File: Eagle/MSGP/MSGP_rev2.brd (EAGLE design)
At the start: 71.8 x 43.9 mm, 42 parts, among them IC1 74ALS04D, IC2 NE5532D, IC3 74ALS04D, IC4 74ALS04D, U1 LTC6905CS5TRMPBF

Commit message: Updates to Layout/Schem
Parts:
- added JP11, JP14, JP15: (no value), jumper:JP1
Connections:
- new net N$15: IC4.14, JP11.1
- new net N$22: IC1.14, JP14.1
- new net N$28: IC3.14, JP15.1
- net VCC: now also JP11.2, JP14.2, JP15.2; no longer IC1.14, IC3.14, IC4.14
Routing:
- net VCC: track 174.4 -> 165.8 mm
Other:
- board size 71.8 x 43.9 mm -> 81 x 57 mm
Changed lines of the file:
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@@
 <board>
 <plain>
-<wire x1="0" y1="0" x2="71.806" y2="0" width="0" layer="20"/>
-<wire x1="71.806" y1="0" x2="71.806" y2="43.932" width="0" layer="20"/>
-<wire x1="71.806" y1="43.932" x2="0" y2="43.932" width="0" layer="20"/>
-<wire x1="0" y1="43.932" x2="0" y2="0" width="0" layer="20"/>
+<wire x1="-8.89" y1="-0.889" x2="71.806" y2="0" width="0" layer="20"/>
+<wire x1="71.806" y1="0" x2="72.06" y2="56.124" width="0" layer="20"/>
+<wire x1="72.06" y1="56.124" x2="-8.89" y2="56.124" width="0" layer="20"/>
+<wire x1="-8.89" y1="56.124" x2="-8.89" y2="-0.889" width="0" layer="20"/>
 </plain>
 <attributes>
@@
 <element name="JP12" library="jumper" package="JP1" value="" x="40.64" y="8.89" rot="R270"/>
 <element name="JP13" library="jumper" package="JP1" value="" x="48.26" y="7.62" rot="R180"/>
+<element name="JP11" library="jumper" package="JP1" value="" x="-24.511" y="1.905"/>
+<element name="JP14" library="jumper" package="JP1" value="" x="-31.369" y="1.905"/>
+<element name="JP15" library="jumper" package="JP1" value="" x="-38.227" y="1.905"/>
 </elements>
 <signals>
 <signal name="GND">
 <polygon width="0.4064" layer="1" isolate="0.3048">
-<vertex x="0.635" y="44.831"/>
-<vertex x="73.533" y="45.339"/>
+<vertex x="-9.779" y="56.515"/>
+<vertex x="73.533" y="56.896"/>
 <vertex x="73.533" y="40.767"/>
 <vertex x="52.832" y="40.64"/>
 <vertex x="52.832" y="15.24"/>
-<vertex x="1.016" y="15.24"/>
+<vertex x="-10.033" y="15.494"/>
 </polygon>
 <polygon width="0.4064" layer="1" isolate="0.254">
-<vertex x="1.016" y="14.478"/>
+<vertex x="-9.144" y="14.478"/>
 <vertex x="54.102" y="14.478"/>
 <vertex x="53.848" y="39.878"/>
 <vertex x="73.406" y="39.878"/>
 <vertex x="72.898" y="0.508"/>
-<vertex x="1.016" y="0.762"/>
+<vertex x="-9.525" y="-0.381"/>
 </polygon>
 <contactref element="IC1" pad="7"/>
@@
 <contactref element="R9" pad="2"/>
 <polygon width="0.4064" layer="16">
-<vertex x="-1.016" y="14.732"/>
-<vertex x="-0.762" y="-1.016"/>
+<vertex x="-10.668" y="14.732"/>
+<vertex x="-10.414" y="-1.016"/>
 <vertex x="73.66" y="-0.254"/>
 <vertex x="73.66" y="2.032"/>
@@
 </polygon>
 <polygon width="0.4064" layer="16">
-<vertex x="-1.016" y="15.24"/>
-<vertex x="-0.762" y="44.196"/>
-<vertex x="72.644" y="44.704"/>
+<vertex x="-9.017" y="15.875"/>
+<vertex x="-10.16" y="57.404"/>
+<vertex x="73.279" y="57.658"/>
 <vertex x="72.644" y="40.894"/>
 <vertex x="52.832" y="40.64"/>
@@
 </signal>
 <signal name="VCC">
-<contactref element="IC1" pad="14"/>
 <contactref element="U1" pad="1"/>
 <contactref element="IC2" pad="8"/>
@@
 <wire x1="23.368" y1="9.628" x2="23.368" y2="9.374" width="0.4064" layer="1"/>
 <wire x1="23.368" y1="9.374" x2="26.924" y2="9.374" width="0.4064" layer="1"/>
-<contactref element="IC3" pad="14"/>
-<contactref element="IC4" pad="14"/>
 <contactref element="JP12" pad="1"/>
 <wire x1="53.34" y1="8.89" x2="55.88" y2="11.43" width="0.4064" layer="16"/>
@@
 <wire x1="32.385" y1="17.145" x2="31.75" y2="17.78" width="0.4064" layer="16"/>
 <wire x1="31.75" y1="17.78" x2="31.75" y2="19.05" width="0.4064" layer="16"/>
-<wire x1="33.7566" y1="33.02" x2="33.02" y2="33.02" width="0.4064" layer="1"/>
 <wire x1="10.922" y1="24.13" x2="16.51" y2="24.13" width="0.4064" layer="16"/>
 <wire x1="16.51" y1="24.13" x2="24.13" y2="16.51" width="0.4064" layer="16"/>
@@
 <via x="31.75" y="19.05" extent="1-16" drill="0.6"/>
 <wire x1="31.75" y1="19.05" x2="33.02" y2="20.32" width="0.4064" layer="1"/>
-<wire x1="33.02" y1="20.32" x2="35.0266" y2="20.32" width="0.4064" layer="1"/>
 <wire x1="38.1" y1="20.32" x2="33.655" y2="15.875" width="0.4064" layer="16"/>
-<wire x1="33.7566" y1="33.02" x2="31.75" y2="33.02" width="0.4064" layer="1"/>
 <wire x1="31.75" y1="33.02" x2="30.48" y2="31.75" width="0.4064" layer="1"/>
 <wire x1="30.48" y1="31.75" x2="30.48" y2="30.48" width="0.4064" layer="1"/>
@@
 <contactref element="JP13" pad="1"/>
 <wire x1="41.91" y1="8.89" x2="48.26" y2="8.89" width="0.4064" layer="1"/>
-<wire x1="10.3886" y1="32.766" x2="12.234" y2="32.766" width="0.4064" layer="1"/>
 <wire x1="12.234" y1="32.766" x2="14" y2="31" width="0.4064" layer="1"/>
 <wire x1="14" y1="31" x2="14" y2="25.43" width="0.4064" layer="1"/>
@@
 <wire x1="3.175" y1="26.797" x2="3.175" y2="27.559" width="0.4064" layer="1"/>
 <wire x1="3.175" y1="27.559" x2="8.382" y2="32.766" width="0.4064" layer="1"/>
-<wire x1="8.382" y1="32.766" x2="10.3886" y2="32.766" width="0.4064" layer="1"/>
 <wire x1="33.274" y1="9.017" x2="32.917" y2="9.374" width="0.4064" layer="1"/>
 <wire x1="32.917" y1="9.374" x2="26.924" y2="9.374" width="0.4064" layer="1"/>
@@
 <wire x1="62.424" y1="23.241" x2="60.071" y2="23.241" width="0.4064" layer="1"/>
 <wire x1="60.071" y1="23.241" x2="59.69" y2="22.86" width="0.4064" layer="1"/>
-<wire x1="39.37" y1="8.89" x2="41.91" y2="8.89" width="0" layer="19" extent="1-1"/>
+<contactref element="JP11" pad="2"/>
+<contactref element="JP14" pad="2"/>
+<contactref element="JP15" pad="2"/>
+<wire x1="-31.369" y1="3.175" x2="-38.227" y2="3.175" width="0" layer="19" extent="1-1"/>
+<wire x1="-24.511" y1="3.175" x2="-31.369" y2="3.175" width="0" layer="19" extent="1-1"/>
+<wire x1="9.144" y1="9.474" x2="-24.511" y2="3.175" width="0" layer="19" extent="1-1"/>
+<wire x1="41.91" y1="8.89" x2="39.37" y2="8.89" width="0" layer="19" extent="1-1"/>
+<wire x1="5.1308" y1="26.0858" x2="7.5692" y2="24.2062" width="0" layer="19" extent="1-1"/>
 </signal>
 <signal name="N$4">
@@
 <wire x1="29.21" y1="20.32" x2="26.67" y2="20.32" width="0.4064" layer="1"/>
 </signal>
+<signal name="N$15">
+<contactref element="IC4" pad="14"/>
+<contactref element="JP11" pad="1"/>
+<wire x1="-24.511" y1="0.635" x2="35.0266" y2="20.32" width="0" layer="19" extent="1-1"/>
+</signal>
+<signal name="N$22">
+<contactref element="JP14" pad="1"/>
+<contactref element="IC1" pad="14"/>
+<wire x1="-31.369" y1="0.635" x2="10.3886" y2="32.766" width="0" layer="19" extent="1-1"/>
+</signal>
+<signal name="N$28">
+<contactref element="IC3" pad="14"/>
+<contactref element="JP15" pad="1"/>
+<wire x1="-38.227" y1="0.635" x2="33.7566" y2="33.02" width="0" layer="19" extent="1-1"/>
+</signal>
 </signals>

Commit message: updated boards
fixed some of the issued we encountered while making the board
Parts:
- moved JP15 67.5 mm to (26.7, 20.3), turned to 180 degrees
- moved JP11 59.2 mm to (31.8, 20.3), turned to 180 degrees
- moved JP14 54.9 mm to (20.3, 20.3), turned to 180 degrees
- moved U1 6.60 mm to (6.35, 31.8)
- moved R6 6.35 mm to (10.8, 31.8)
- moved IC1 6.35 mm to (13.5, 42.9)
- moved IC3 6.35 mm to (36.8, 43.2)
- moved IC4 6.35 mm to (38.1, 30.5)
- moved R10 6.35 mm to (27.9, 47.0)
- moved R11 6.35 mm to (45.7, 47.0)
- moved R12 6.35 mm to (27.9, 43.2)
- moved R14 6.35 mm to (47.0, 26.7)
- moved R15 6.35 mm to (47.0, 30.5)
- moved R16 6.35 mm to (25.4, 35.6)
- moved R18 6.35 mm to (29.2, 30.5)
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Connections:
- removed net GND: C1.2, C2.2, C3.2, C4.2, C5.2, IC1.7, IC2.3, IC2.4, IC2.5, IC3.7, IC4.7, JP1.2, JP13.2, JP2.1, JP4.2, JP5.1, JP5.2, JP6.1, JP6.2, JP7.2, R1.2, R10.2, R11.2, R12.2, R13.2, R14.2, R15.2, R16.2, R17.2, R18.2, R19.2, R2.2, R3.2, R4.2, R5.2, R7.2, R8.2, R9.2, U1.2, USBMINI.GND
- new net GNDA: C1.2, C2.2, C3.2, C4.2, C5.2, IC2.3, IC2.4, IC2.5, JP1.2, JP13.2, JP2.1, JP4.2, JP5.2, JP6.2, JP7.2, U1.2, USBMINI.GND
- new net GND_D: IC1.7, IC3.7, IC4.7, JP5.1, JP6.1, R1.2, R10.2, R11.2, R12.2, R13.2, R14.2, R15.2, R16.2, R17.2, R18.2, R19.2, R2.2, R3.2, R4.2, R5.2, R7.2, R8.2, R9.2
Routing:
- net VCC: track 165.8 -> 138.5 mm, vias 3 -> 1
- net GNDA: track 0.00 -> 24.1 mm
- net N$22: track 0.00 -> 22.8 mm, vias 0 -> 2
- net N$28: track 0.00 -> 21.1 mm, vias 0 -> 1
- net N$15: track 0.00 -> 7.61 mm
- net N$1: track 134.1 -> 126.4 mm
- added copper zone on layer 1, net GNDA
- added copper zone on layer 16, net GNDA
- added copper zone on layer 1, net GND_D
- added copper zone on layer 16, net GND_D
- removed copper zone on layer 1, net GND
- removed copper zone on layer 16, net GND
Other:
- board size 81 x 57 mm -> 72.1 x 57.1 mm

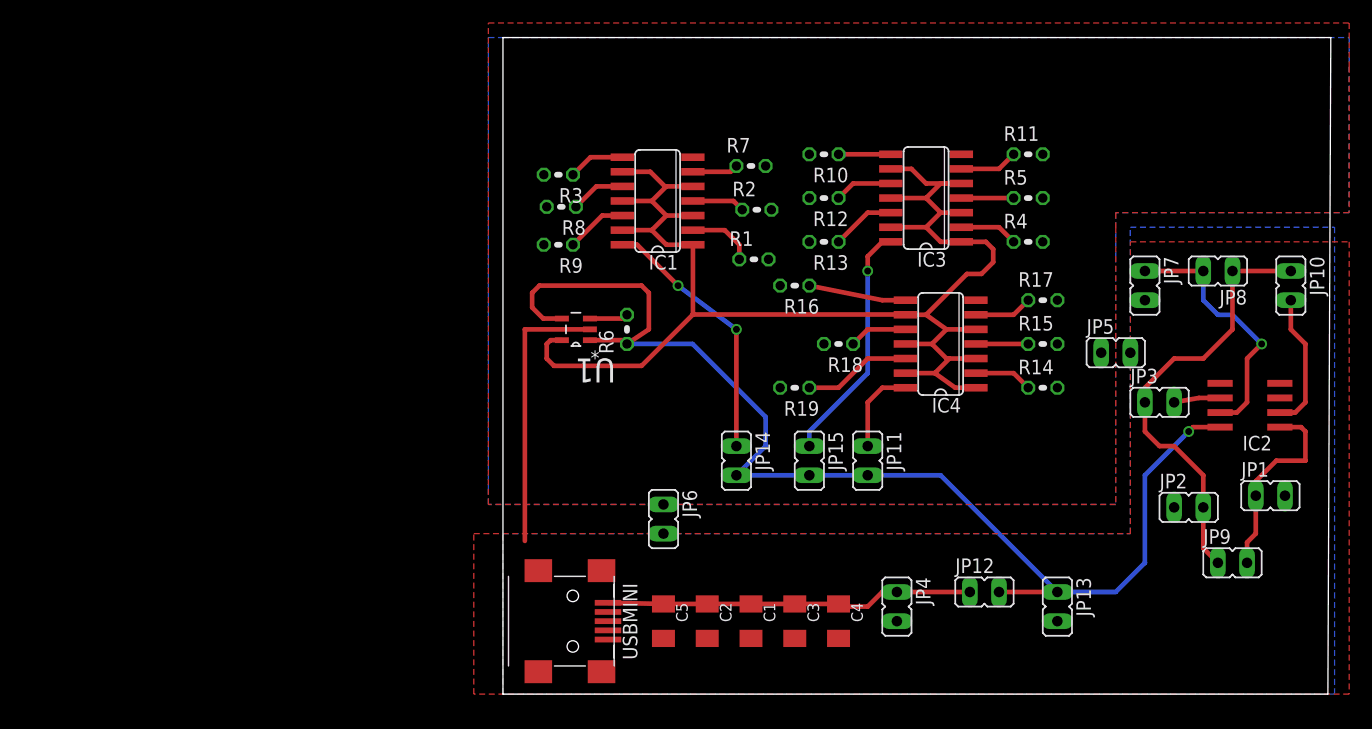
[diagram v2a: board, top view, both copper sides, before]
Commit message: minor changes to MSGP rev2
change one trace to digital ground
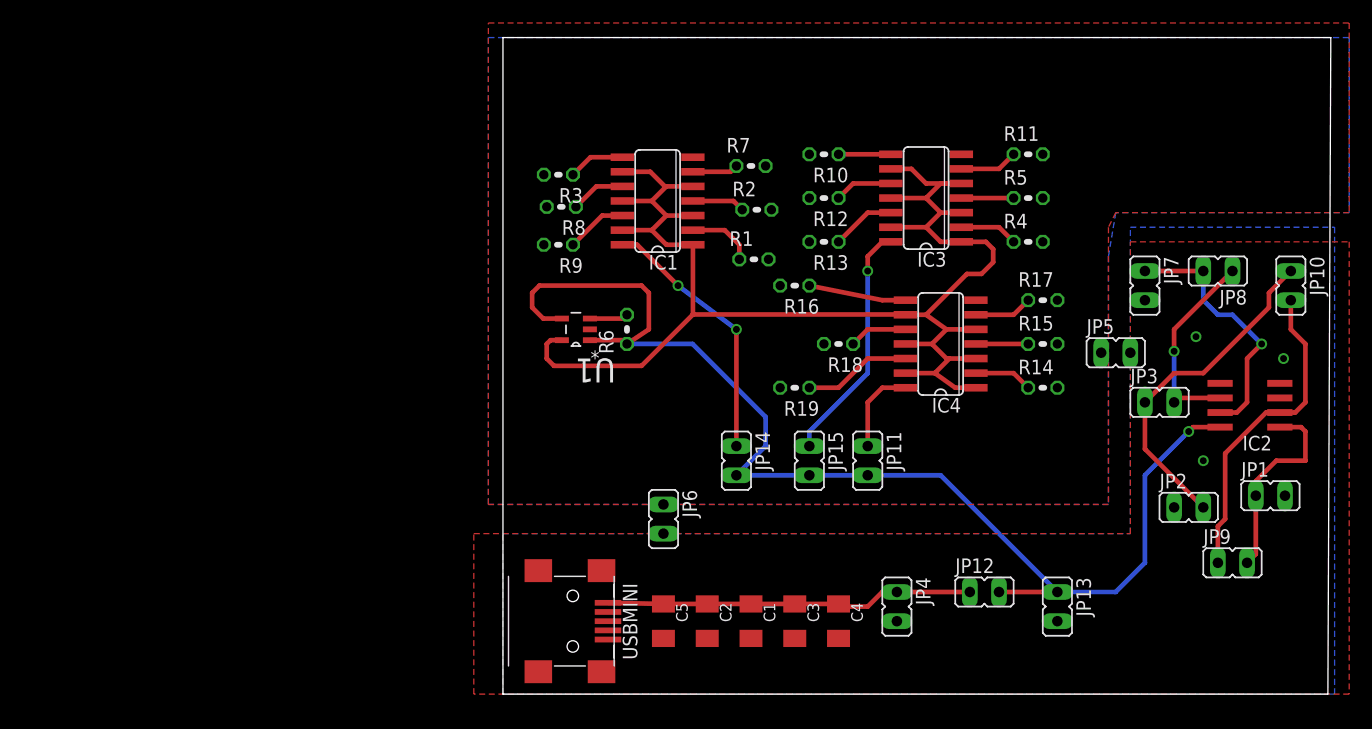
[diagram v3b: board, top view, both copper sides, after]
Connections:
- removed net N$13: IC2.6, JP3.2
- new net N$30: JP10.1, JP2.2, JP3.1
- net GNDA: no longer U1.2
- net GND_D: now also U1.2
- net N$2: now also IC2.6, JP3.2; no longer JP10.1, JP2.2, JP3.1, JP9.1
- net N$5: now also JP9.1
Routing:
- net N$30: track 0.00 -> 29.4 mm
- net GNDA: track 24.1 -> 0.00 mm, vias 0 -> 2
- net N$2: track 38.5 -> 17.7 mm, vias 0 -> 1
- net N$5: track 12.0 -> 28.0 mm
- net N$13: track 4.04 -> 0.00 mm
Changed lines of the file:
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@@
 </signal>
 <signal name="N$2">
-<contactref element="JP2" pad="2"/>
-<contactref element="JP9" pad="1"/>
-<contactref element="JP10" pad="1"/>
-<contactref element="JP3" pad="1"/>
 <contactref element="JP8" pad="1"/>
-<wire x1="63.5" y1="31.75" x2="63.5" y2="36.83" width="0.4064" layer="1"/>
-<wire x1="63.5" y1="36.83" x2="68.58" y2="36.83" width="0.4064" layer="1"/>
-<wire x1="55.88" y1="25.4" x2="55.88" y2="26.67" width="0.4064" layer="1"/>
-<wire x1="55.88" y1="26.67" x2="58.42" y2="29.21" width="0.4064" layer="1"/>
-<wire x1="58.42" y1="29.21" x2="60.96" y2="29.21" width="0.4064" layer="1"/>
-<wire x1="60.96" y1="29.21" x2="63.5" y2="31.75" width="0.4064" layer="1"/>
-<wire x1="55.88" y1="25.4" x2="55.88" y2="22.86" width="0.4064" layer="1"/>
-<wire x1="55.88" y1="22.86" x2="57.15" y2="21.59" width="0.4064" layer="1"/>
-<wire x1="57.15" y1="21.59" x2="58.42" y2="21.59" width="0.4064" layer="1"/>
-<wire x1="58.42" y1="21.59" x2="60.96" y2="19.05" width="0.4064" layer="1"/>
-<wire x1="60.96" y1="19.05" x2="60.96" y2="16.256" width="0.4064" layer="1"/>
-<wire x1="60.96" y1="16.256" x2="60.96" y2="12.7" width="0.4064" layer="1"/>
-<wire x1="60.96" y1="12.7" x2="62.23" y2="11.43" width="0.4064" layer="1"/>
+<contactref element="IC2" pad="6"/>
+<contactref element="JP3" pad="2"/>
+<wire x1="62.424" y1="25.781" x2="58.801" y2="25.781" width="0.4064" layer="1"/>
+<wire x1="58.801" y1="25.781" x2="58.42" y2="25.4" width="0.4064" layer="1"/>
+<wire x1="63.5" y1="36.83" x2="58.42" y2="31.75" width="0.4064" layer="1"/>
+<wire x1="58.42" y1="31.75" x2="58.42" y2="29.845" width="0.4064" layer="1"/>
+<via x="58.42" y="29.845" extent="1-16" drill="0.6" shape="square"/>
+<wire x1="58.42" y1="29.845" x2="58.42" y2="25.4" width="0.4064" layer="16"/>
 </signal>
 <signal name="N$3">
 <contactref element="IC2" pad="1"/>
 <contactref element="JP1" pad="1"/>
-<contactref element="JP9" pad="2"/>
 <wire x1="67.624" y1="23.241" x2="69.469" y2="23.241" width="0.4064" layer="1"/>
 <wire x1="69.469" y1="23.241" x2="69.85" y2="22.86" width="0.4064" layer="1"/>
@@
 <wire x1="65.532" y1="17.272" x2="65.532" y2="18.542" width="0.4064" layer="1"/>
 <wire x1="65.532" y1="18.542" x2="67.31" y2="20.32" width="0.4064" layer="1"/>
-<wire x1="64.77" y1="11.43" x2="64.77" y2="13.208" width="0.4064" layer="1"/>
-<wire x1="64.77" y1="13.208" x2="65.532" y2="13.97" width="0.4064" layer="1"/>
-<wire x1="65.532" y1="13.97" x2="65.532" y2="17.272" width="0.4064" layer="1"/>
+<contactref element="JP9" pad="2"/>
+<wire x1="64.77" y1="11.43" x2="65.532" y2="12.192" width="0.4064" layer="1"/>
+<wire x1="65.532" y1="12.192" x2="65.532" y2="17.272" width="0.4064" layer="1"/>
 </signal>
 <signal name="N$5">
@@
 <wire x1="68.58" y1="34.29" x2="68.58" y2="31.75" width="0.4064" layer="1"/>
 <wire x1="68.58" y1="31.75" x2="69.85" y2="30.48" width="0.4064" layer="1"/>
+<contactref element="JP9" pad="1"/>
+<wire x1="62.23" y1="11.43" x2="62.23" y2="14.605" width="0.4064" layer="1"/>
+<wire x1="62.23" y1="14.605" x2="62.865" y2="15.24" width="0.4064" layer="1"/>
+<wire x1="62.865" y1="15.24" x2="62.865" y2="20.955" width="0.4064" layer="1"/>
+<wire x1="62.865" y1="20.955" x2="66.421" y2="24.511" width="0.4064" layer="1"/>
+<wire x1="66.421" y1="24.511" x2="67.624" y2="24.511" width="0.4064" layer="1"/>
 </signal>
 <signal name="N$6">
@@
 <wire x1="60.96" y1="34.29" x2="62.23" y2="33.02" width="0.4064" layer="16"/>
 <wire x1="62.23" y1="33.02" x2="63.5" y2="33.02" width="0.4064" layer="16"/>
-</signal>
-<signal name="N$13">
-<contactref element="IC2" pad="6"/>
-<contactref element="JP3" pad="2"/>
-<wire x1="62.424" y1="25.781" x2="60.579" y2="25.781" width="0.4064" layer="1"/>
-<wire x1="60.579" y1="25.781" x2="58.42" y2="25.4" width="0.4064" layer="1"/>
 </signal>
 <signal name="N$14">
@@
 <contactref element="IC2" pad="5"/>
 <contactref element="IC2" pad="3"/>
-<contactref element="U1" pad="2"/>
 <polygon width="0.4064" layer="16">
 <vertex x="0" y="13.97"/>
@@
 <vertex x="0" y="0"/>
 </polygon>
-<wire x1="7.5692" y1="31.75" x2="1.905" y2="31.75" width="0.4064" layer="1"/>
-<wire x1="1.905" y1="31.75" x2="1.905" y2="13.335" width="0.4064" layer="1"/>
+<via x="60.325" y="31.115" extent="1-16" drill="0.6" shape="square"/>
+<via x="67.945" y="29.21" extent="1-16" drill="0.6" shape="square"/>
 </signal>
 <signal name="GND_D">
@@
 <vertex x="-1.27" y="58.42"/>
 <vertex x="73.66" y="58.42"/>
-<vertex x="73.66" y="54.61"/>
 <vertex x="73.66" y="41.91"/>
 <vertex x="53.34" y="41.91"/>
-<vertex x="53.34" y="40.64"/>
-<vertex x="53.34" y="16.51"/>
+<vertex x="52.705" y="40.64"/>
+<vertex x="52.705" y="16.51"/>
 <vertex x="-1.27" y="16.51"/>
 </polygon>
 <polygon width="0.4064" layer="16">
-<vertex x="0" y="57.15"/>
+<vertex x="-1.27" y="57.15"/>
 <vertex x="73.66" y="57.15"/>
 <vertex x="73.66" y="41.91"/>
 <vertex x="53.34" y="41.91"/>
-<vertex x="53.34" y="38.1"/>
-<vertex x="53.34" y="16.51"/>
+<vertex x="52.705" y="38.1"/>
+<vertex x="52.705" y="16.51"/>
 <vertex x="-1.27" y="16.51"/>
-<vertex x="-1.27" y="17.78"/>
-<vertex x="-1.27" y="57.15"/>
-</polygon>
+</polygon>
+<contactref element="U1" pad="2"/>
+</signal>
+<signal name="N$30">
+<contactref element="JP10" pad="1"/>
+<contactref element="JP2" pad="2"/>
+<contactref element="JP3" pad="1"/>
+<wire x1="55.88" y1="25.4" x2="55.88" y2="21.336" width="0.4064" layer="1"/>
+<wire x1="55.88" y1="21.336" x2="60.96" y2="16.256" width="0.4064" layer="1"/>
+<wire x1="55.88" y1="25.4" x2="58.42" y2="27.94" width="0.4064" layer="1"/>
+<wire x1="58.42" y1="27.94" x2="60.96" y2="27.94" width="0.4064" layer="1"/>
+<wire x1="60.96" y1="27.94" x2="66.675" y2="33.655" width="0.4064" layer="1"/>
+<wire x1="66.675" y1="33.655" x2="66.675" y2="34.925" width="0.4064" layer="1"/>
+<wire x1="66.675" y1="34.925" x2="68.58" y2="36.83" width="0.4064" layer="1"/>
+</signal>
+<signal name="N$31">
+<via x="60.96" y="20.32" extent="1-16" drill="0.6" shape="square"/>
 </signal>
 </signals>
